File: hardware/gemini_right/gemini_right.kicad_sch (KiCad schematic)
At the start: 80 parts, among them IC1 CW2015CHBD, IC2 XL9555__TSSOP-24_, J1 Conn_01x06_MountingPin, J1_toLeft1 USB_C_Receptacle_USB2.0_16P, J2 Conn_01x02_MountingPin, J2_toHost1 USB_C_Receptacle_USB2.0_16P, SW1 SW_Push, SW10 SW_Push, SW11 SW_Push, SW12 SW_Push, SW13 SW_Push, SW14 SW_Push, SW15 SW_Push, SW16 SW_Push, SW17 SW_Push, SW18 SW_Push, SW19 SW_Push, SW2 SW_Push, SW20 SW_Push, SW3 SW_Push, SW4 SW_Push, SW5 SW_Push, SW6 SW_Push, SW7 SW_Push, SW8 SW_Push, SW9 SW_Push, U1 ETA9742, U2 XC6206PxxxMR, U3 CH582F, Y1 32.768khz 12.5pF 20ppm, Y2 32Mhz 12pF 10ppm

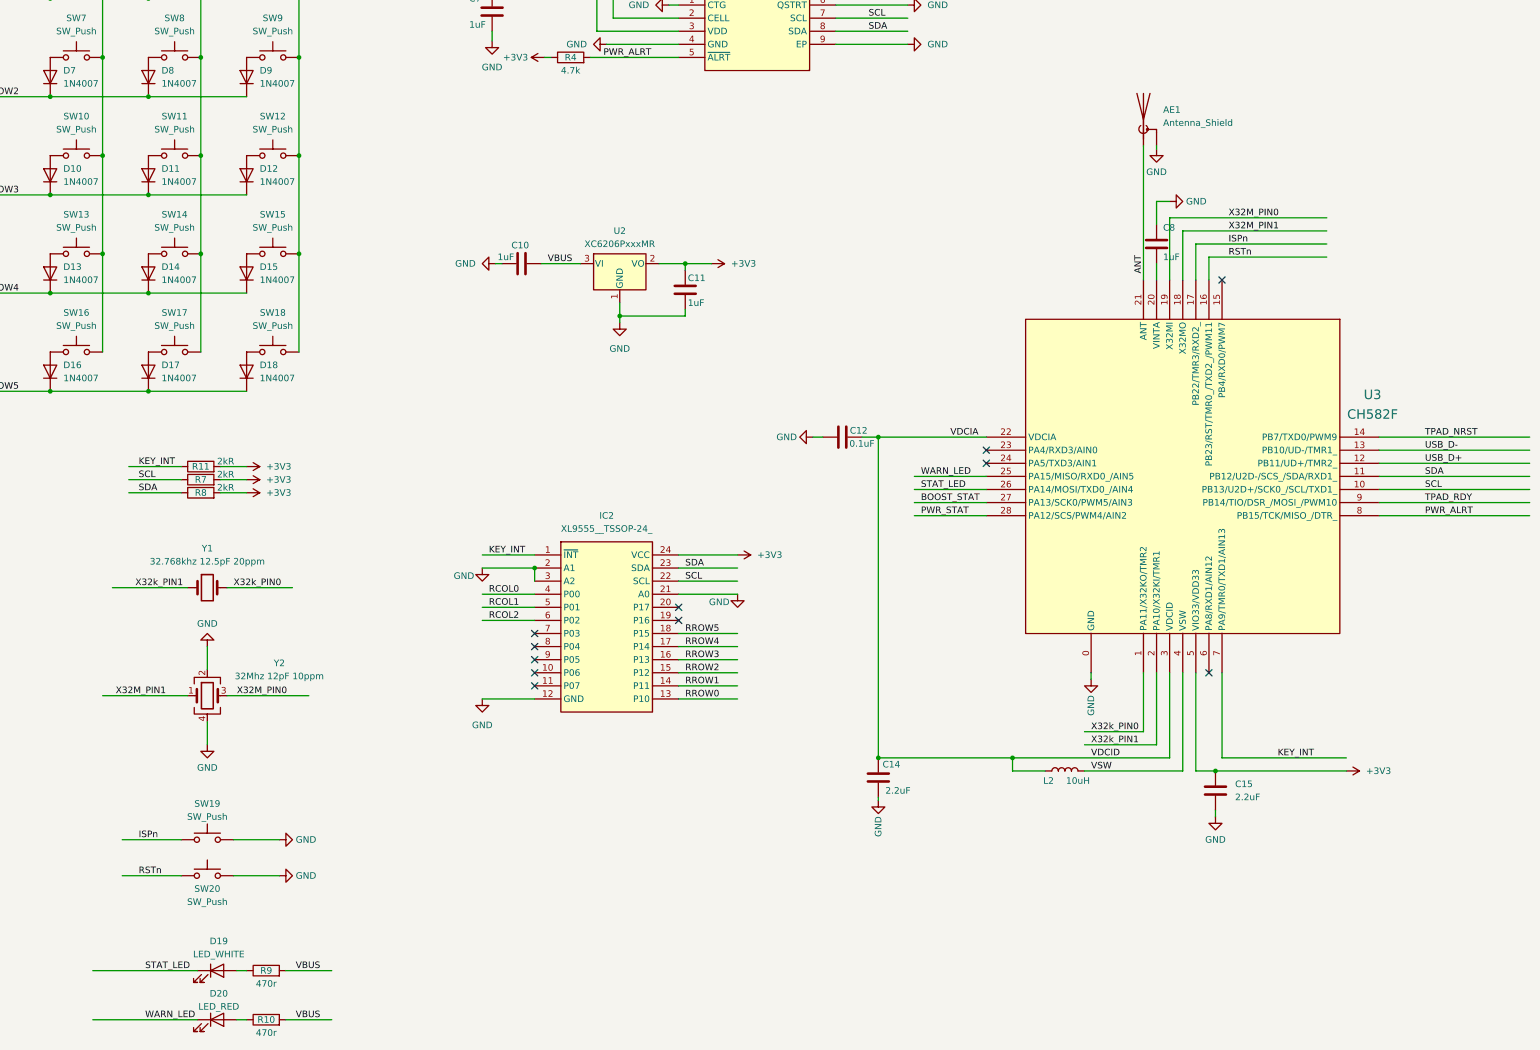
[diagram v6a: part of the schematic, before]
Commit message: use esp32c3 instead
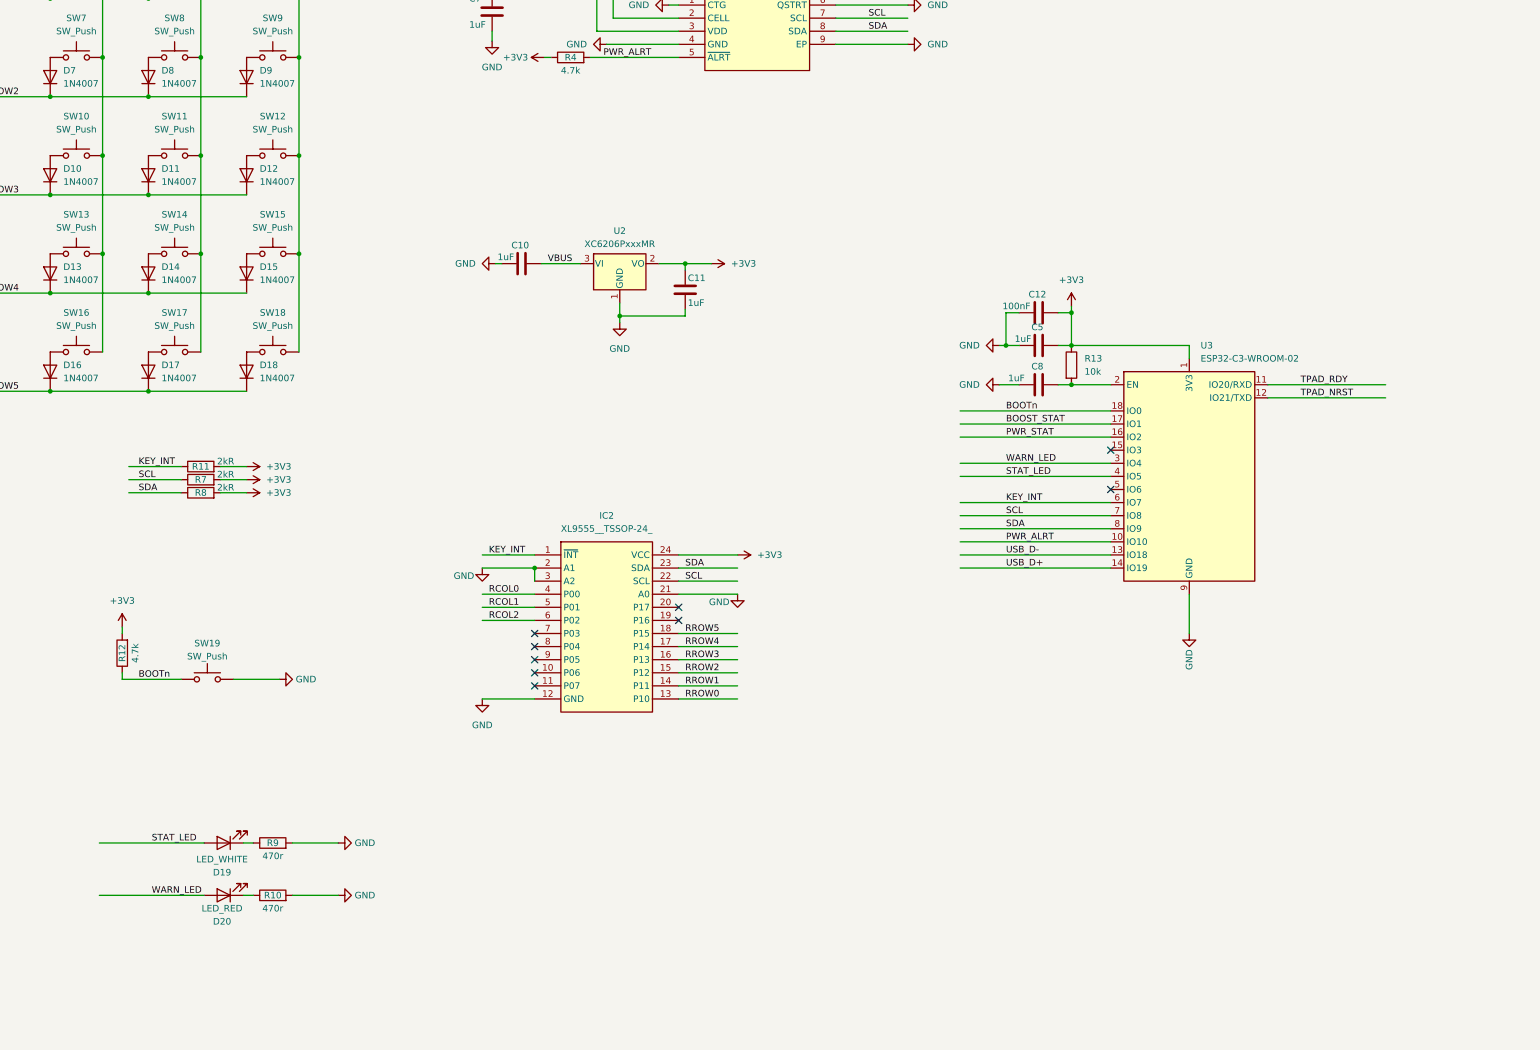
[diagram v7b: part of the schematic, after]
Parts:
- removed AE1: Antenna_Shield, chxxx_antenna:ANT-F-3-2.4G-1.6mmFR4-WCH_mirror, symbol Device:Antenna_Shield
- removed C14, C15: 2.2uF, Capacitor_SMD:C_0603_1608Metric_Pad1.08x0.95mm_HandSolder, symbol Device:C
- removed L2: 10uH, Inductor_SMD:L_Chilisin_BMRA00040420, symbol Device:L
- removed SW20: SW_Push, Button_Switch_SMD:SW_Tactile_SPST_NO_Straight_CK_PTS636Sx25SMTRLFS, symbol Switch:SW_Push
- removed U3: CH582F, chxxx:QFN28_4X4, symbol chxxx:CH582F
- removed Y1: 32.768khz 12.5pF 20ppm, Crystal:Crystal_SMD_3215-2Pin_3.2x1.5mm, symbol Device:Crystal
- removed Y2: 32Mhz 12pF 10ppm, Crystal:Crystal_SMD_3225-4Pin_3.2x2.5mm, symbol Device:Crystal_GND24
- added C5: 1uF, Capacitor_SMD:C_0603_1608Metric_Pad1.08x0.95mm_HandSolder, symbol Device:C
- added R12: 4.7k, Resistor_SMD:R_0603_1608Metric_Pad0.98x0.95mm_HandSolder, symbol Device:R
- added R13: 10k, Resistor_SMD:R_0603_1608Metric_Pad0.98x0.95mm_HandSolder, symbol Device:R
- added U3: ESP32-C3-WROOM-02, RF_Module:ESP32-C3-WROOM-02, symbol RF_Module:ESP32-C3-WROOM-02
- C12: value 0.1uF -> 100nF
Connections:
- net VDCIA is gone; now on net +3V3: C12.2
- net +3V3: now also C5.2, R12.2, R13.1, U3.1 (3V3)
- net BOOST_STAT: now also U3.17 (IO1)
- net GND: now also R10.2, R9.2, C5.1, U3.19 (GND), U3.9 (GND)
- net KEY_INT: now also U3.6 (IO7)
- net PWR_ALRT: now also U3.10 (IO10)
- net PWR_STAT: now also U3.16 (IO2)
- net SCL: now also U3.7 (IO8)
- net SDA: now also U3.8 (IO9)
- net STAT_LED: now also D19.2 (A), U3.4 (IO5); no longer D19.1 (K)
- net TPAD_NRST: now also U3.12 (IO21/TXD)
- net TPAD_RDY: now also U3.11 (IO20/RXD)
- net USB_D+: now also U3.14 (IO19)
- net USB_D-: now also U3.13 (IO18)
- net VBUS: no longer R10.2, R9.2
- net WARN_LED: now also D20.2 (A), U3.3 (IO4); no longer D20.1 (K)
- net at C8.2: now also R13.2, U3.2 (EN)
- net at R9.1: now also D19.1 (K); no longer D19.2 (A)
- net at R10.1: now also D20.1 (K); no longer D20.2 (A)
- net ISPn renamed BOOTn
- net BOOTn: now also R12.1, U3.18 (IO0)
- no-connect marks 14 -> 12
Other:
- moved on the sheet: D19, D20, R10, R9, SW19
